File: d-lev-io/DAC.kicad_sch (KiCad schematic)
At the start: 29 parts, among them IC1 ES9010K2M, IC3 MAX97220C/MAX97220D, X1 7M-50.000MAAJ-T

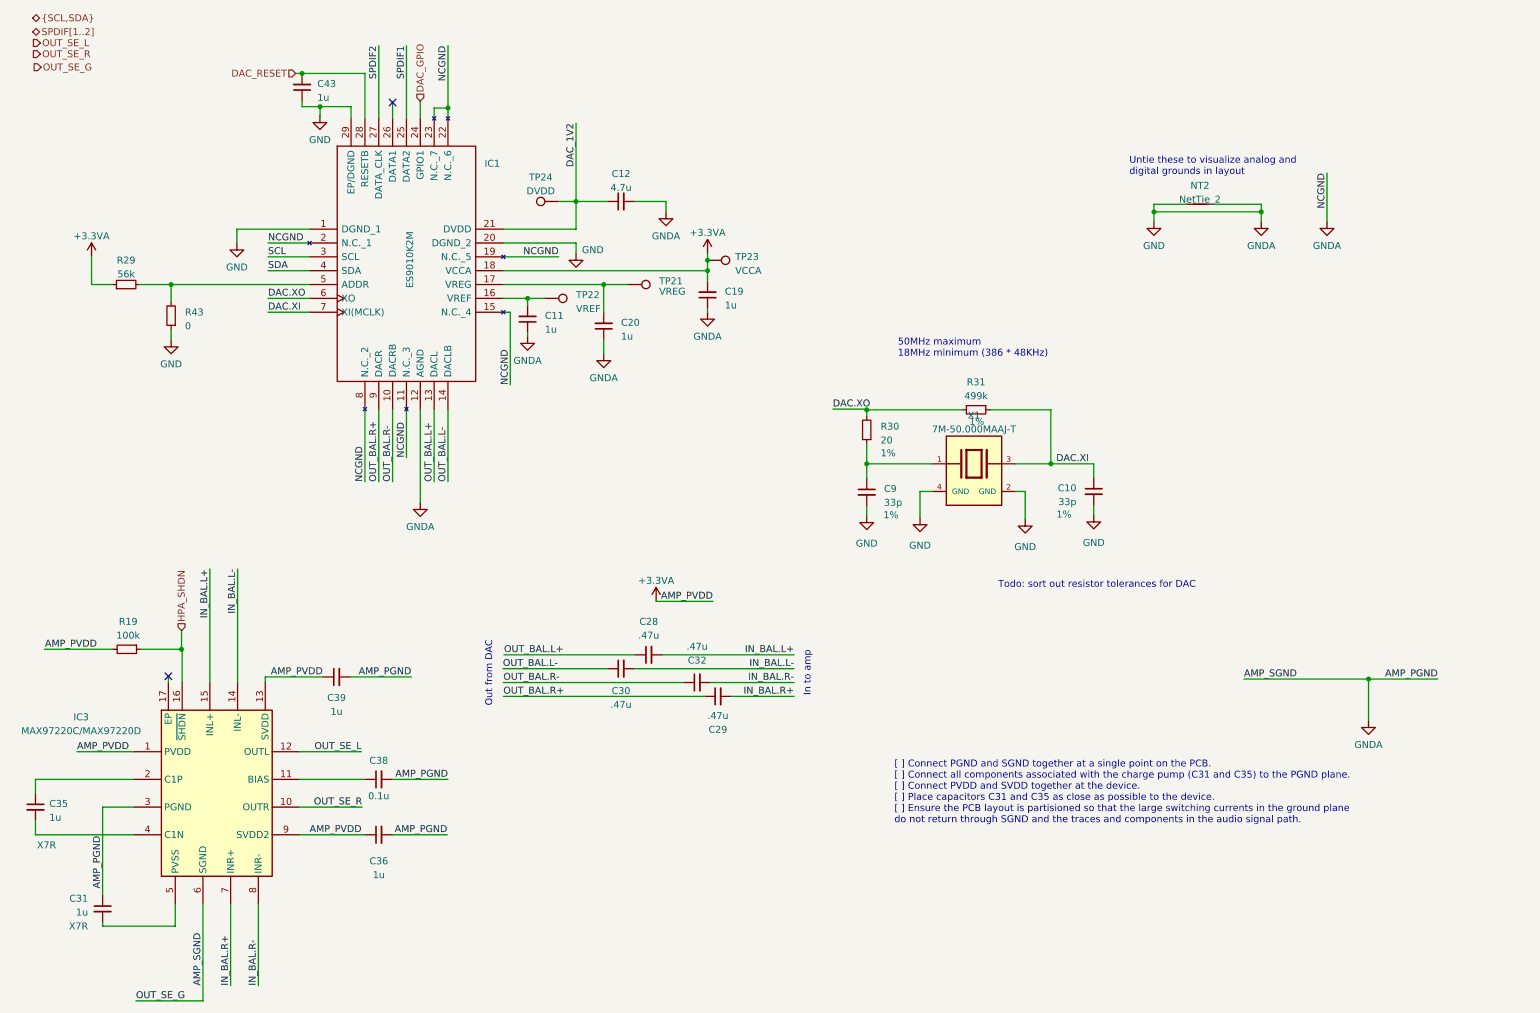
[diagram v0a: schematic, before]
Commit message: I/O board silk placement
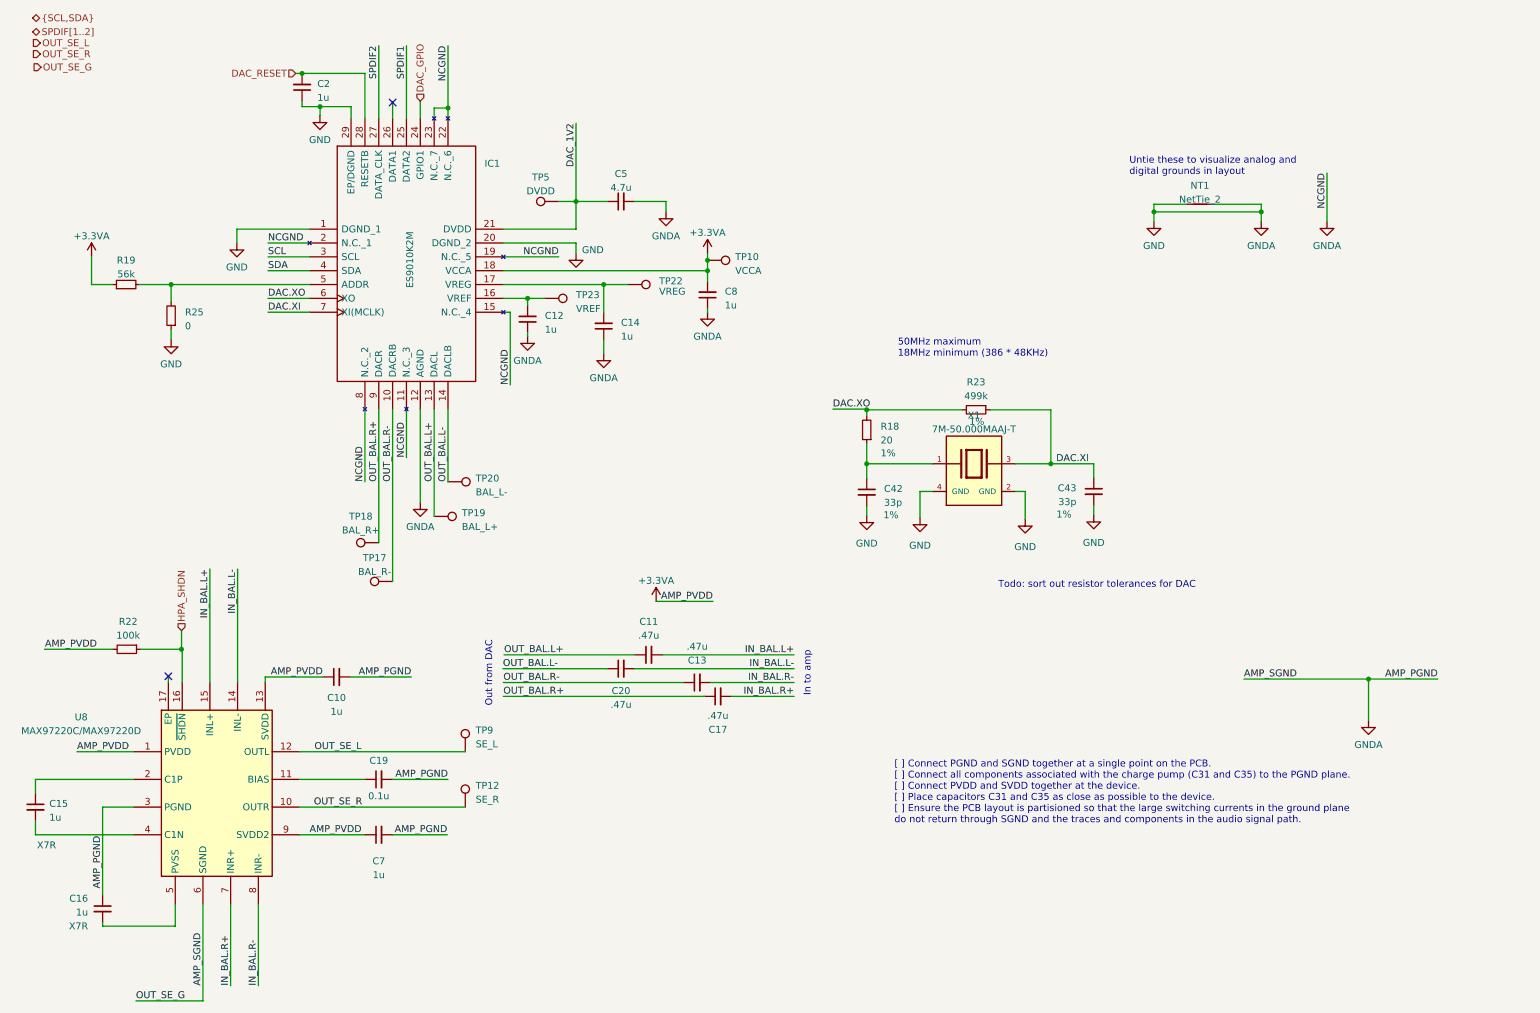
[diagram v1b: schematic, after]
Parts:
- added TP12: SE_R, TestPoint:TestPoint_Pad_D1.5mm, symbol Connector:TestPoint
- added TP17: BAL_R-, TestPoint:TestPoint_Pad_D1.5mm, symbol Connector:TestPoint
- added TP18: BAL_R+, TestPoint:TestPoint_Pad_D1.5mm, symbol Connector:TestPoint
- added TP19: BAL_L+, TestPoint:TestPoint_Pad_D1.5mm, symbol Connector:TestPoint
- added TP20: BAL_L-, TestPoint:TestPoint_Pad_D1.5mm, symbol Connector:TestPoint
- added TP9: SE_L, TestPoint:TestPoint_Pad_D1.5mm, symbol Connector:TestPoint
- renumbered C39 to C10, C28 to C11, C11 to C12, C32 to C13, C20 to C14, C35 to C15, C31 to C16, C29 to C17, C38 to C19, C43 to C2, C30 to C20, C9 to C42, C10 to C43, C12 to C5, C36 to C7, C19 to C8, NT2 to NT1, R30 to R18, R29 to R19, R19 to R22, R31 to R23, R43 to R25, TP23 to TP10, TP21 to TP22, TP22 to TP23, TP24 to TP5, IC3 to U8
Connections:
- net OUT_BAL.L+: now also TP19.1
- net OUT_BAL.L-: now also TP20.1
- net OUT_BAL.R+: now also TP18.1
- net OUT_BAL.R-: now also TP17.1
- net OUT_SE_L: now also TP9.1
- net OUT_SE_R: now also TP12.1

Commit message: Add iBOMs and additional part numbers
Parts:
- C10, C12, C14, C2, C7, C8: MPN (none) -> CL10B105KP8NNNC; Notes (none) -> Common; Supplier (none) -> Digi-Key; Supplier URL (none) -> https://www.digikey.com/en/products/detail/samsung-electro-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
- C11, C13, C17, C20: value .47u -> 470n; MPN (none) -> 0603B474K100CT; Notes (none) -> Common; Supplier (none) -> Digi-Key; Supplier URL (none) -> https://www.digikey.com/en/products/detail/walsin-technolog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
- C15, C16: ESR <100m -> (none); MPN (none) -> C1608X7R1C105K080AC; Notes (none) -> X7R 100m ESR; Supplier (none) -> Digi-Key; Supplier URL (none) -> https://www.digikey.com/en/products/detail/tdk-corporation/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; Type X7R -> (none)
- C19: value 0.1u -> 100n; MPN (none) -> GRM188R71E104KA01D; Notes (none) -> Common; Supplier (none) -> Digi-Key; Supplier URL (none) -> https://www.digikey.com/en/products/detail/murata-electroni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
- C42, C43: Supplier (none) -> Mouser; Supplier URL (none) -> https://www.mouser.com/ProductDetail/603-CC603FRNPO0BN330
- C5: MPN (none) -> CL10B475KQ8NQNC; Notes (none) -> Common; Supplier (none) -> Digi-Key; Supplier Alt (none) -> Mouser; Supplier Alt URL (none) -> https://www.mouser.com/ProductDetail/187-CL10B475KQ8NQNC; Supplier URL (none) -> https://www.digikey.com/en/products/detail/samsung-electro-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
- IC1: Height 0.9 -> (none); MPN (none) -> ES9010K2M; Manufacturer_Name ESS Technology -> (none); Manufacturer_Part_Number ES9010K2M -> (none); Supplier (none) -> Mouser; Supplier URL (none) -> https://www.mouser.com/ProductDetail/460-ES9010K2M
- NT1: DNP (none) -> Y
- R18: MPN (none) -> CR0603FX-20R0ELF; Supplier (none) -> Mouser; Supplier URL (none) -> https://www.mouser.com/ProductDetail/652-CR0603FX-20R0ELF
- R19: MPN (none) -> RC0603JR-0756KL; Supplier (none) -> Digi-Key; Supplier URL (none) -> https://www.digikey.com/en/products/detail/yageo/RC0603JR-0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
- R23: MPN (none) -> CR0603FX-4993ELF; Supplier (none) -> Mouser; Supplier URL (none) -> https://www.mouser.com/ProductDetail/652-CR0603FX-4993ELF
- R25: MPN (none) -> RMCF0603ZT0R00; Supplier (none) -> Digi-Key; Supplier URL (none) -> https://www.digikey.com/en/products/detail/stackpole-electr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; now not fitted
- TP10: value VCCA -> TestPoint; DNP (none) -> Y
- TP12: value SE_R -> TestPoint; DNP (none) -> Y
- TP17: value BAL_R- -> TestPoint; DNP (none) -> Y
- TP18: value BAL_R+ -> TestPoint; DNP (none) -> Y
- TP19: value BAL_L+ -> TestPoint; DNP (none) -> Y
- TP20: value BAL_L- -> TestPoint; DNP (none) -> Y
- TP22: value VREG -> TestPoint; DNP (none) -> Y
- TP23: value VREF -> TestPoint; DNP (none) -> Y
- TP5: value DVDD -> TestPoint; DNP (none) -> Y
- TP9: value SE_L -> TestPoint; DNP (none) -> Y
- U8: Height 0.8 -> (none); MPN (none) -> MAX97220DETE+T; Manufacturer_Name Analog Devices -> (none); Manufacturer_Part_Number MAX97220AETE+T -> (none); Mouser Part Number 700-MAX97220AETE+T -> (none); Mouser Price/Stock https://www.mouser.co.uk/ProductDetail/Maxim-Integrated/MAX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 -> (none); Notes (none) -> C/D version; Supplier (none) -> Mouser; Supplier URL (none) -> https://www.mouser.com/ProductDetail/700-MAX97220DETE%2bT
- X1: MANUFACTURER TXC CORPORATION -> (none); MPN (none) -> 7M-50.000MAAJ-T; Supplier (none) -> Mouser; Supplier URL (none) -> https://www.mouser.com/ProductDetail/717-7M-50.000MAAJ-T
